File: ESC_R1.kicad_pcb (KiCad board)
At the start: 4 copper layers, 239 parts, among them J101 Conn_01x02_Pin, J102 Conn_01x02_Pin, J103 Conn_01x02_Pin, J201 SM05B-GHS-TB, J202 SWD TagConnect, J203 SM06B-GHS-TB, J204 SM04B-GHS-TB, J301 SM03B-GHS-TB, J401 USB_C_Receptacle_USB2.0, J801 XT60PW-F, J802 XT60PW-M, Q501 BSC072N08NS5, Q502 BSC072N08NS5, Q601 BSC072N08NS5, Q602 BSC072N08NS5, Q701 BSC072N08NS5, Q702 BSC072N08NS5, SW201 PTS810 SJK, U101 LMR36006, U102 LMR36006, U103 TLV75533PDBV, U104 TLV75533PDBV, U201 STM32F446RETx, U301 TJA1441AT, U401 USBLC6-2SC6, U501 IR2171S, U502 INA180B2, U601 IR2171S, U602 INA180B2, U701 IR2171S, U702 INA180B2, Y201 16MHz

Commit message: chore: project update
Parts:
- moved R701 1.99 mm to (179.7, 49.2)
- moved R702 1.99 mm to (179.7, 50.5)
- moved R706 1.99 mm to (180.6, 49.3)
- moved R707 1.99 mm to (180.6, 51.0)
- moved C701 1.99 mm to (181.8, 48.7)
- moved C702 1.99 mm to (181.8, 51.1)
- moved C704 0.85 mm to (190.8, 52.2)
- moved D701 0.85 mm to (189.3, 48.4)
- moved C705 0.85 mm to (190.7, 50.9)
- moved R703 0.85 mm to (187.9, 51.2)
- moved U701 0.85 mm to (188.7, 50.3)
- moved C703 0.58 mm to (190.8, 53.8)
- moved C707 0.35 mm to (186.2, 57.6)
- moved U702 0.35 mm to (188.9, 57.0)
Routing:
- net /[7] 3-Phase Bridge - Phase C/PH_CIN+: track 2.76 -> 23.9 mm, vias 1 -> 2
- net /[7] 3-Phase Bridge - Phase C/PH_VS: track 16.2 -> 0.32 mm, vias 2 -> 0
- net +12V: track 35.5 -> 30.6 mm
- net /[7] 3-Phase Bridge - Phase C/PH_IR_HIN: track 7.68 -> 2.86 mm
- net /[7] 3-Phase Bridge - Phase C/PH_IR_LIN: track 7.68 -> 2.86 mm
- net GND: track 89.9 -> 86.2 mm, vias 76 -> 75

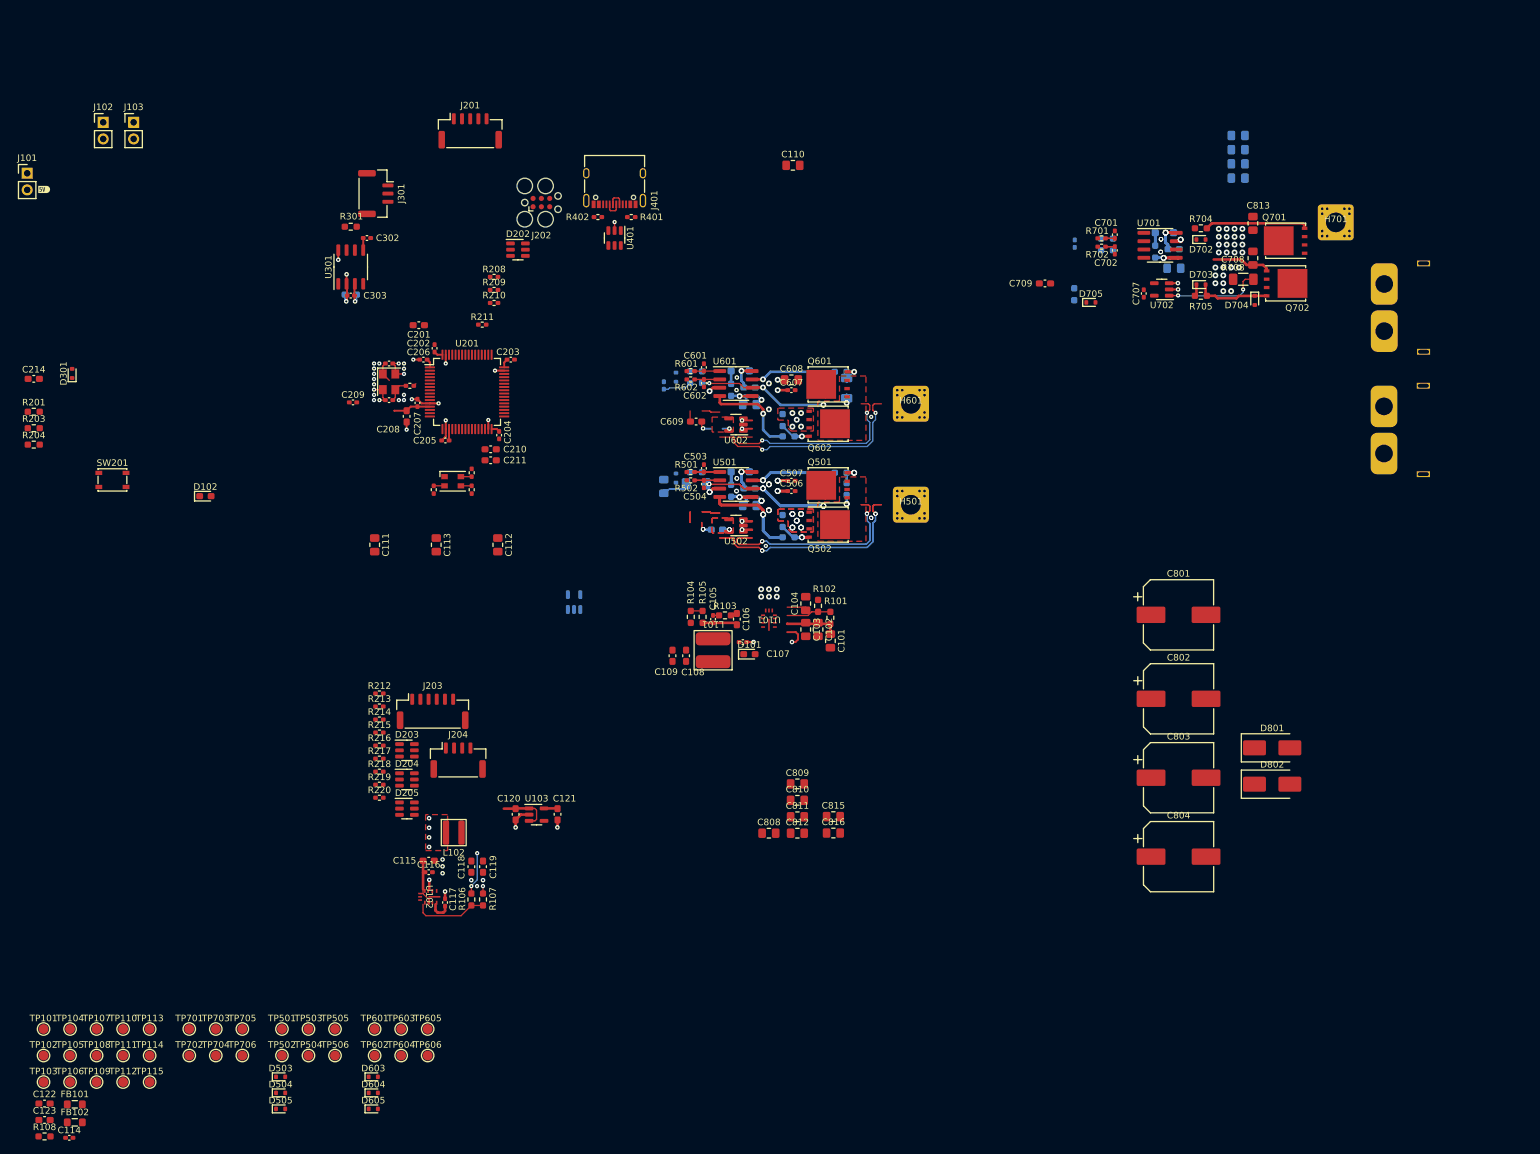
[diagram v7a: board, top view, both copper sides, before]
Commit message: feat: finished inverter placement and routing
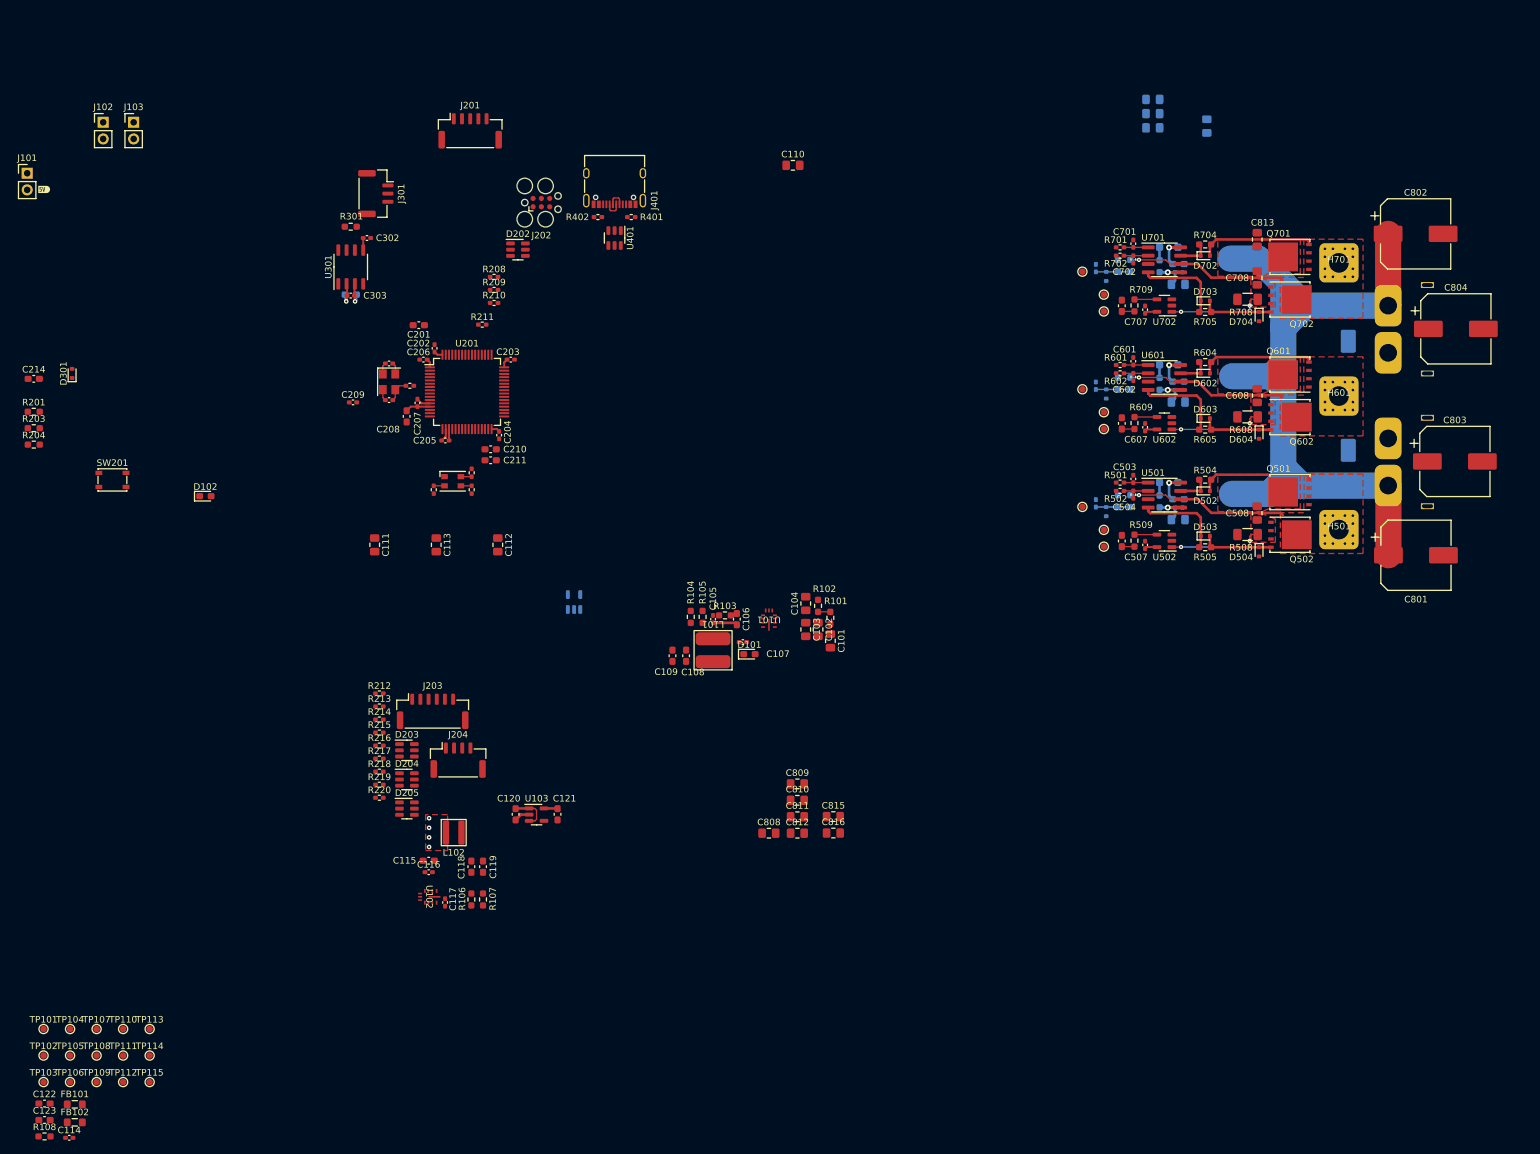
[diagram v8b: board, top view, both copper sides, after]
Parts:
- removed the TP501 at (54.6, 169.9)
- removed the TP502 at (54.6, 174.0)
- removed TP506, TP606, TP706: GND, TestPoint:TestPoint_Pad_D1.5mm
- removed the TP601 at (68.7, 169.9)
- removed the TP602 at (68.7, 174.0)
- removed the TP701 at (40.4, 169.9)
- removed the TP702 at (40.4, 174.0)
- C506, D505, D605, D705, D801, D802: moved to B.Cu
- C508, C509, D502, D602, R504, R505, R508, R509, R604, R605, R608, R609, R709: moved to F.Cu
- H501, H601, H701: footprint TestPoint:Pad_5.5x5.5mm -> TestPoint:HC_Phase_Pad_6x6
- TP101, TP102, TP103, TP104, TP105, TP106, TP107, TP108, TP109, TP110, TP111, TP112, TP113, TP114, TP115: footprint TestPoint:TestPoint_Pad_D1.5mm -> TestPoint:TestPoint_Pad_D1.0mm
- TP501: renamed from TP503; footprint TestPoint:TestPoint_Pad_D1.5mm -> TestPoint:TestPoint_Pad_D1.0mm
- TP502: renamed from TP504; footprint TestPoint:TestPoint_Pad_D1.5mm -> TestPoint:TestPoint_Pad_D1.0mm
- TP503: renamed from TP505; footprint TestPoint:TestPoint_Pad_D1.5mm -> TestPoint:TestPoint_Pad_D1.0mm
- TP601: renamed from TP603; footprint TestPoint:TestPoint_Pad_D1.5mm -> TestPoint:TestPoint_Pad_D1.0mm
- TP602: renamed from TP604; footprint TestPoint:TestPoint_Pad_D1.5mm -> TestPoint:TestPoint_Pad_D1.0mm
- TP603: renamed from TP605; footprint TestPoint:TestPoint_Pad_D1.5mm -> TestPoint:TestPoint_Pad_D1.0mm
- TP701: renamed from TP703; footprint TestPoint:TestPoint_Pad_D1.5mm -> TestPoint:TestPoint_Pad_D1.0mm
- TP702: renamed from TP704; footprint TestPoint:TestPoint_Pad_D1.5mm -> TestPoint:TestPoint_Pad_D1.0mm
- TP703: renamed from TP705; footprint TestPoint:TestPoint_Pad_D1.5mm -> TestPoint:TestPoint_Pad_D1.0mm
- moved TP702 178.4 mm to (176.8, 54.3)
- moved TP701 174.3 mm to (180.1, 60.4)
- moved TP703 172.8 mm to (180.1, 57.8)
- moved D504 170.7 mm to (203.8, 97.1), turned to -90 degrees
- moved D604 168.5 mm to (203.8, 79.1), turned to -90 degrees
- moved D503 163.6 mm to (195.6, 94.7)
- moved D603 162.0 mm to (195.6, 76.7)
- moved D605 156.3 mm to (180.4, 73.0), turned to 90 degrees
- moved D505 155.6 mm to (180.4, 91.0), turned to 90 degrees
- moved TP602 145.5 mm to (176.8, 72.3)
- moved TP502 144.8 mm to (176.8, 90.2)
- moved TP501 142.0 mm to (180.1, 96.3)
- moved TP601 141.1 mm to (180.1, 78.3)
- moved TP503 140.0 mm to (180.1, 93.7)
- moved TP603 139.7 mm to (180.1, 75.8)
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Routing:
- net (no net): track 122.4 -> 0.00 mm, vias 40 -> 0
- net +BATT: track 9.58 -> 125.7 mm, vias 17 -> 0
- net /[5] 3-Phase Bridge - Phase A/PH_CIN+: track 104.3 -> 14.6 mm, vias 10 -> 2
- net GND: track 86.2 -> 17.5 mm, vias 75 -> 1
- net /[5] 3-Phase Bridge - Phase A/PH_VS: track 0.00 -> 24.5 mm, vias 0 -> 1
- net /[7] 3-Phase Bridge - Phase C/PH_VS: track 0.32 -> 24.5 mm, vias 0 -> 1
- net /[5] 3-Phase Bridge - Phase A/PH_HOUT: track 26.2 -> 4.55 mm, vias 2 -> 0
- net /[5] 3-Phase Bridge - Phase A/PH_LOUT: track 31.9 -> 13.3 mm, vias 4 -> 0
- net /[6] 3-Phase Bridge - Phase B/PH_CIN+: track 30.9 -> 14.6 mm
- net /[6] 3-Phase Bridge - Phase B/PH_HOUT_G: track 3.81 -> 17.4 mm, vias 1 -> 0
- net /[7] 3-Phase Bridge - Phase C/PH_LOUT: track 1.81 -> 13.3 mm
- net +12V: track 30.6 -> 19.1 mm, vias 5 -> 3
- net /[1] Power Supply/VSW_12V: track 10.6 -> 0.00 mm, vias 2 -> 0
- net /[5] 3-Phase Bridge - Phase A/PH_HOUT_G: track 7.61 -> 17.4 mm, vias 2 -> 0
- net /[7] 3-Phase Bridge - Phase C/PH_CIN+: track 23.9 -> 14.6 mm
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- added copper zone on F.Cu, net +BATT
- added copper zone on F.Cu, net /[5] 3-Phase Bridge - Phase A/PH_VS
- added copper zone on F.Cu, net /[6] 3-Phase Bridge - Phase B/PH_VS
- added copper zone on F.Cu, net /[7] 3-Phase Bridge - Phase C/PH_CIN+
- added copper zone on F.Cu, net /[7] 3-Phase Bridge - Phase C/PH_VS
- removed copper zone on F.Cu, net +3.3V
- removed copper zone on F.Cu, net GND
